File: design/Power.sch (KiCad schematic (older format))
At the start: 47 parts, among them U2 TC2117, U3 DRV8302

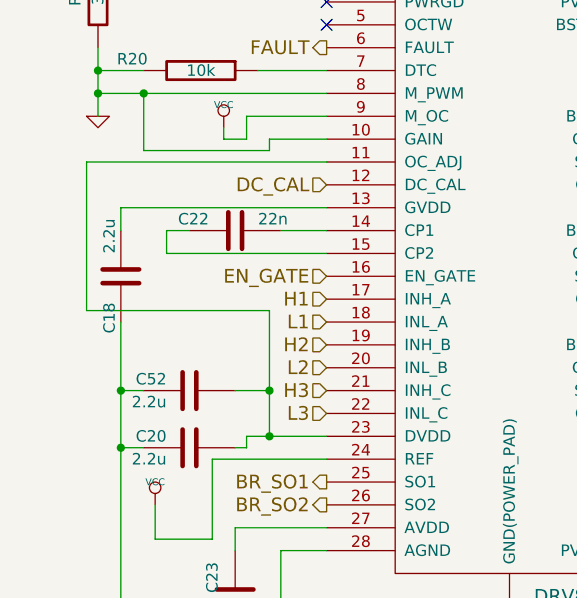
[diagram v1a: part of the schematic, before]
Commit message: HW 4.12: Added another capacitor to GVDD in the DRV8302
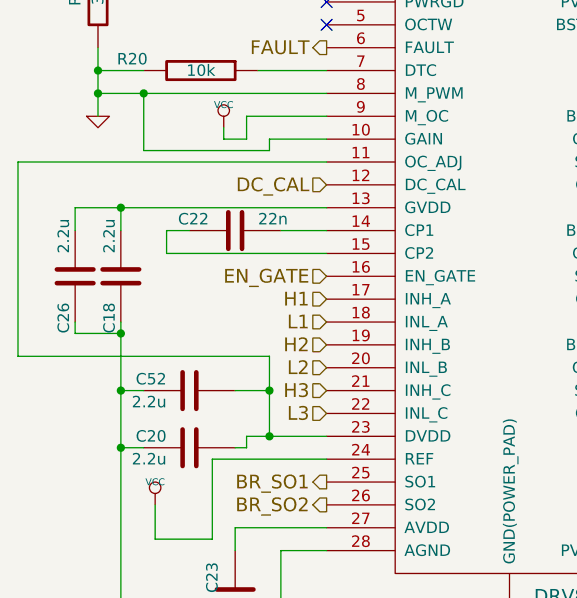
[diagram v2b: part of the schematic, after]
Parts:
- added C26: 2.2u, CRF1:SMD-0603_c, symbol C-RESCUE-BLDC_4
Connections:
- net GND: now also C26.2
- net at C18.1, U3.13 (GVDD): now also C26.1
